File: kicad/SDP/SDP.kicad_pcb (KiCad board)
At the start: 4 copper layers, 164 parts, among them J1 GPIO, J10 Limit, J11 Conn_01x07, J12 Conn_01x07, J13 Conn_01x03, J14 Conn_01x03, J15 Conn_01x02, J16 Conn_01x02, J17 Conn_01x04, J18 Conn_01x04, J19 Conn_01x04, J2 SPI, J20 Conn_01x04, J21 Conn_01x04, J22 Conn_01x04, J23 Conn_01x02, J24 POWER, J25 Conn_01x04, J3 UART, J4 I2C, J5 Conn_01x04, J6 Conn_01x04, J7 RJ25, J8 Conn_01x07, J9 Conn_01x07, Q1 IRLZ44N, Q2 IRLZ44N, Q3 IRLZ44N, SW1 SW_Push_Dual, U1 TPS54233, U2 TPS54233, U3 PIC24FJ128GA010-I/PT, U4 DS3231SN-T&R, Y1 8MHz, Y2 32.768kHz

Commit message: PCB layout and schematic updates
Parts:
- added J26: Conn_01x02, TerminalBlock_Phoenix:TerminalBlock_Phoenix_PT-1,5-2-5.0-H_1x02_P5.00mm_Horizontal, F.Cu at (153.5, 50.2)
- D6, D7, D8: value 1N4007 -> SS1200; footprint Diode_THT:D_DO-41_SOD81_P10.16mm_Horizontal -> Diode_SMD:D_SMA
- J1: footprint Connector_PinSocket_2.54mm:PinSocket_2x12_P2.54mm_Vertical -> Connector_PinSocket_2.54mm:PinSocket_2x09_P2.54mm_Vertical
- Q1, Q2, Q3: footprint Package_TO_SOT_THT:TO-220-3_Vertical -> Package_TO_SOT_SMD:TO-263-2
- moved J11 365.1 mm to (55.3, 135.8)
- moved J12 365.1 mm to (64.5, 135.8)
- moved J8 365.1 mm to (59.9, 135.8)
- moved J9 365.1 mm to (50.7, 135.8)
- moved R18 359.3 mm to (64.9, 99.4), turned to -90 degrees
- moved J6 351.9 mm to (69.0, 160.8)
- moved R22 338.0 mm to (101.6, 90.7), turned to 90 degrees
- moved J13 336.3 mm to (80.5, 162.8)
- moved J14 336.3 mm to (85.1, 162.8)
- moved J10 336.1 mm to (96.5, 85.5), turned to 90 degrees
- moved R23 335.6 mm to (104.1, 90.7), turned to 90 degrees
- moved R24 332.8 mm to (106.7, 90.7), turned to 90 degrees
- moved R21 329.5 mm to (99.1, 90.7), turned to 90 degrees
- moved R20 327.6 mm to (96.5, 90.7), turned to 90 degrees
- moved C22 326.2 mm to (65.4, 162.1), turned to -90 degrees
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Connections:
- J1 pad 1: P21_RB4 -> P19_RE9
- J1 pad 10: P97_RG13 -> P68_RD8
- J1 pad 11: P95_RG14 -> P67_RA15
- J1 pad 12: P1_RG15 -> P69_RD9
- J1 pad 13: P66_RA14 -> P70_RD10
- J1 pad 14: P67_RA15 -> P71_RD11
- J1 pad 15: P93_RE0 -> P89_RG1
- J1 pad 16: P94_RE1 -> P90_RG0
- J1 pad 17: P98_RE2 -> P93_RE0
- J1 pad 18: P99_RE3 -> P94_RE1
- J1 pad 2: P20_RB5 -> P18_RE8
- J1 pad 3: P68_RD8 -> P21_RB4
- J1 pad 4: P69_RD9 -> P20_RB5
- J1 pad 5: P70_RD10 -> P1_RG15
- J1 pad 6: P71_RD11 -> P3_RE5
- J1 pad 7: P90_RG0 -> P4_RE6
- J1 pad 8: P89_RG1 -> P5_RE7
- J1 pad 9: P96_RG12 -> P66_RA14
- J10 pad 1: P93_LIMIT -> P100_LIMIT
- J10 pad 11: P93_LIMIT -> P95_LIMIT
- J10 pad 3: P93_LIMIT -> P99_LIMIT
- J10 pad 5: P93_LIMIT -> P98_LIMIT
- J10 pad 7: P93_LIMIT -> P97_LIMIT
- J10 pad 9: P93_LIMIT -> P96_LIMIT
- J2 pad 2: P53_SDO1 -> P14_SS2
- J2 pad 3: P54_SDI1 -> P53_SDO1
- J2 pad 4: P55_SCK1 -> P12_SDO2
- J2 pad 5: P14_SS2 -> P54_SDI1
- J2 pad 6: P12_SDO2 -> P11_SDI2
- J2 pad 7: P11_SDI2 -> P55_SCK1
- J24 pad 2: +3V3 -> GND
- J24 pad 4: +3V3 -> GND
- J24 pad 5: GND -> +3V3
- J24 pad 7: GND -> +3V3
- J3 pad 2: P49_U2RX -> P51_U1TX
- J3 pad 3: P48_U1RTS -> P49_U2RX
- J3 pad 4: P47_U1CTS -> P52_U1RX
- J3 pad 5: P51_U1TX -> P48_U1RTS
- J3 pad 6: P52_U1RX -> P39_U2RTS
- J3 pad 7: P39_U2RTS -> P47_U1CTS
- J4 pad 2: P57_SCL1 -> P59_SDA2
- J4 pad 3: P59_SDA2 -> P57_SCL1
- R20 pad 2: P93_LIMIT -> P100_LIMIT
- R21 pad 2: P93_LIMIT -> P99_LIMIT
- R22 pad 2: P93_LIMIT -> P98_LIMIT
- R23 pad 2: P93_LIMIT -> P97_LIMIT
- R24 pad 2: P93_LIMIT -> P96_LIMIT
- R25 pad 2: P93_LIMIT -> P95_LIMIT
- U3 pad 100: P100_RE4 -> P100_LIMIT
- U3 pad 95: P95_RG14 -> P95_LIMIT
- U3 pad 96: P96_RG12 -> P96_LIMIT
- U3 pad 97: P97_RG13 -> P97_LIMIT
- U3 pad 98: P98_RE2 -> P98_LIMIT
- U3 pad 99: P99_RE3 -> P99_LIMIT

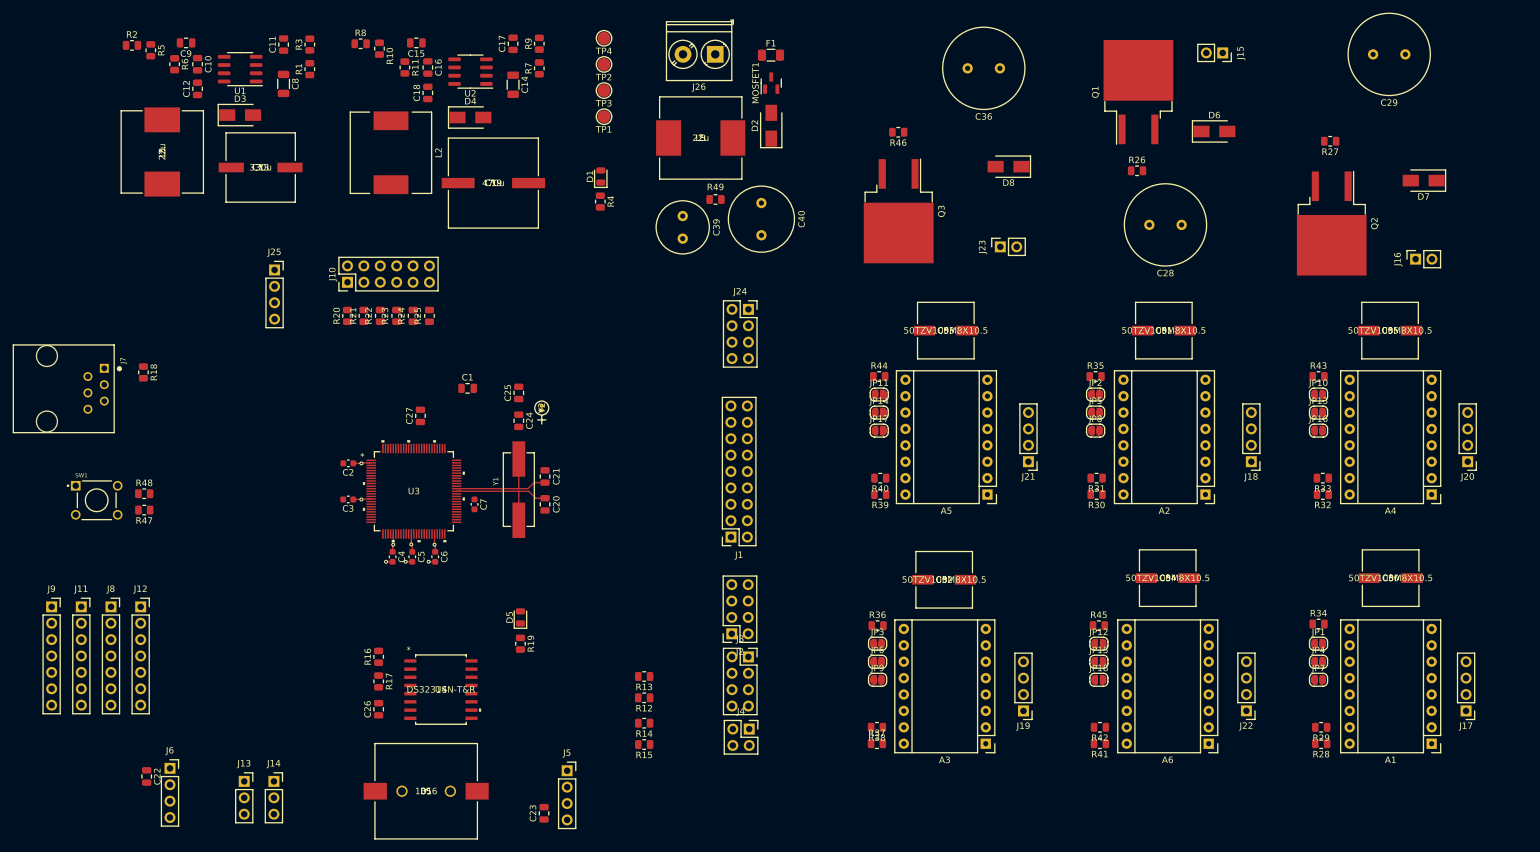
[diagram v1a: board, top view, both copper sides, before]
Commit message: Separated control and motor boards
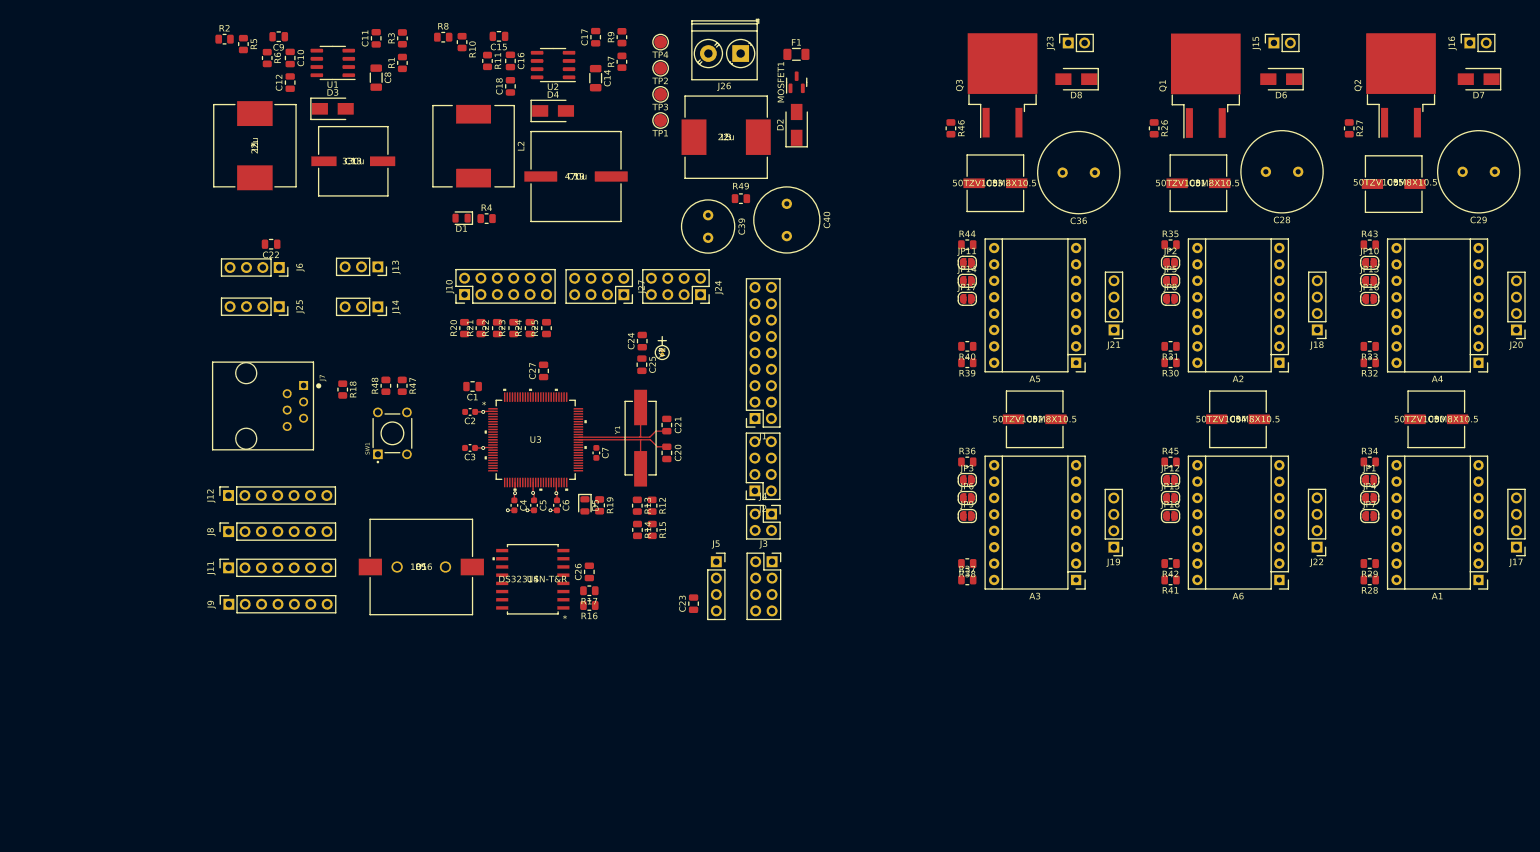
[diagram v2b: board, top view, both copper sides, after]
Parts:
- added J27: MOTOR, Connector_PinSocket_2.54mm:PinSocket_2x04_P2.54mm_Vertical, F.Cu at (139.3, 87.4)
- moved C22 84.7 mm to (84.7, 79.6), turned to 180 degrees
- moved J13 82.4 mm to (101.2, 83.1), turned to -90 degrees
- moved J6 79.4 mm to (85.9, 83.2), turned to -90 degrees
- moved J14 75.3 mm to (101.2, 89.3), turned to -90 degrees
- moved SW1 47.0 mm to (103.5, 108.9), turned to 90 degrees
- moved R47 44.4 mm to (105.0, 101.5), turned to -90 degrees
- moved R48 41.0 mm to (102.5, 101.5), turned to 90 degrees
- moved C23 39.9 mm to (150.1, 135.3)
- moved J5 39.8 mm to (153.7, 128.8)
- moved C26 39.0 mm to (134.0, 130.4)
- moved R17 35.5 mm to (134.0, 133.3), turned to 180 degrees
- moved B1 34.8 mm to (108.0, 129.6)
- moved J16 34.5 mm to (270.4, 48.4)
- moved R16 33.6 mm to (134.0, 135.6), turned to 180 degrees
- moved J4 33.5 mm to (162.2, 121.4)
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
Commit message: PCB layout of main controller board
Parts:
- removed A1, A2, A3, A4, A5, A6: Pololu_Breakout_A4988, Module:Pololu_Breakout-16_15.2x20.3mm
- removed C28, C29, C36: 470u, Capacitor_THT:C_Radial_D12.5mm_H20.0mm_P5.00mm
- removed C30, C31, C32, C33, C34, C35: 50TZV100M8X10.5, 50TZV100M:50TZV100M8X10.5
- removed D6, D7, D8: SS1200, Diode_SMD:D_SMA
- removed J15, J16, J23: Conn_01x02, Connector_PinSocket_2.54mm:PinSocket_1x02_P2.54mm_Vertical
- removed J17, J18, J19, J20, J21, J22: Conn_01x04, Connector_PinHeader_2.54mm:PinHeader_1x04_P2.54mm_Vertical
- removed JP1, JP10, JP11, JP12, JP2, JP3: JP_MS1, Jumper:SolderJumper-2_P1.3mm_Open_RoundedPad1.0x1.5mm
- removed JP13, JP14, JP15, JP4, JP5, JP6: JP_MS2, Jumper:SolderJumper-2_P1.3mm_Open_RoundedPad1.0x1.5mm
- removed JP16, JP17, JP18, JP7, JP8, JP9: JP_MS3, Jumper:SolderJumper-2_P1.3mm_Open_RoundedPad1.0x1.5mm
- removed Q1, Q2, Q3: IRLZ44N, Package_TO_SOT_SMD:TO-263-2
- removed R26, R27, R28, R29, R30, R31, R32, R33, R37, R38, R39, R40, R41, R42, R46: 10k, Resistor_SMD:R_0805_2012Metric
- removed R34, R35, R36, R43, R44, R45: 100k, Resistor_SMD:R_0805_2012Metric
- added H1: MountingHole_Pad, MountingHole:MountingHole_3.2mm_M3_Pad, F.Cu at (77.5, 49.5)
- added H2: MountingHole_Pad, MountingHole:MountingHole_3.2mm_M3_Pad, F.Cu at (166.5, 49.5)
- added H3: MountingHole_Pad, MountingHole:MountingHole_3.2mm_M3_Pad, F.Cu at (166.5, 138.5)
- added H4: MountingHole_Pad, MountingHole:MountingHole_3.2mm_M3_Pad, F.Cu at (77.5, 138.5)
- J27: footprint Connector_PinSocket_2.54mm:PinSocket_2x04_P2.54mm_Vertical -> Connector_PinSocket_2.54mm:PinSocket_2x08_P2.54mm_Vertical
- moved J27 52.8 mm to (133.0, 139.9)
- moved J24 52.7 mm to (145.7, 139.9)
- moved R25 50.2 mm to (97.5, 132.9), turned to -90 degrees
- moved J10 50.1 mm to (110.2, 137.3), turned to -90 degrees
- moved R24 47.3 mm to (100.0, 132.9), turned to -90 degrees
- moved R23 44.9 mm to (102.5, 132.9), turned to -90 degrees
- moved C39 43.7 mm to (108.7, 75.7)
- moved R22 42.9 mm to (105.1, 132.9), turned to -90 degrees
- moved R49 42.4 mm to (115.1, 73.9)
- moved L3 42.1 mm to (113.1, 63.2)
- moved C40 41.7 mm to (122.9, 74.0)
- moved R21 41.4 mm to (107.6, 132.9), turned to -90 degrees
- moved R20 40.6 mm to (110.2, 132.9), turned to -90 degrees
- moved D2 39.9 mm to (126.3, 63.2), turned to 0 degrees
- moved TP4 38.1 mm to (165.0, 80.8), turned to 90 degrees
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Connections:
- J27 pad 1: P72_FAN -> +3V3
- J27 pad 2: P76_EN -> +3V3
- J27 pad 3: P77_STEP -> P72_FAN
- J27 pad 4: P78_DIR -> P76_EN
- J27 pad 5: P79_EN -> P77_STEP
- J27 pad 6: P80_STEP -> P78_DIR
- J27 pad 7: P81_DIR -> P79_EN
- J27 pad 8: P82_EN -> P80_STEP
- J4 pad 1: P56_SDA1 -> P59_SDA2
- J4 pad 2: P59_SDA2 -> P57_SCL1
- J4 pad 3: P57_SCL1 -> P58_SCL2
- J4 pad 4: P58_SCL2 -> P56_SDA1
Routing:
- net P57_SCL1: track 0.00 -> 143.8 mm, vias 0 -> 1
- net P56_SDA1: track 0.00 -> 139.3 mm, vias 0 -> 1
- net P44_TOF4_GPIO1: track 0.00 -> 77.1 mm, vias 0 -> 1
- net P95_LIMIT: track 0.00 -> 72.9 mm, vias 0 -> 2
- net P96_LIMIT: track 0.00 -> 69.7 mm, vias 0 -> 2
- net P35_TOF4_CE: track 0.00 -> 66.6 mm, vias 0 -> 1
- net P97_LIMIT: track 0.00 -> 66.4 mm, vias 0 -> 2
- net P43_TOF3_GPIO1: track 0.00 -> 66.2 mm, vias 0 -> 1
- net P34_TOF3_CE: track 0.00 -> 65.6 mm, vias 0 -> 1
- net P42_TOF2_GPIO1: track 0.00 -> 64.6 mm, vias 0 -> 1
- net P98_LIMIT: track 0.00 -> 62.5 mm, vias 0 -> 2
- net P99_LIMIT: track 0.00 -> 61.0 mm, vias 0 -> 2
- net P41_TOF1_GPIO1: track 0.00 -> 60.4 mm, vias 0 -> 1
- net P100_LIMIT: track 0.00 -> 59.9 mm, vias 0 -> 2
- net P33_TOF2_CE: track 0.00 -> 54.4 mm, vias 0 -> 1
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- added copper zone on In2.Cu, net +3V3
- added copper zone on F.Cu, net GND
- added copper zone on In1.Cu, net GND
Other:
- board outline added: 98 x 98 mm

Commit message: Controller PCB layout
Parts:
- removed J2: SPI, Connector_PinSocket_2.54mm:PinSocket_2x04_P2.54mm_Vertical
- moved R5 120.2 mm to (167.9, 133.0), turned to 180 degrees
- moved R2 117.6 mm to (168.7, 130.0), turned to -90 degrees
- moved C9 117.5 mm to (159.7, 139.3), turned to 0 degrees
- moved R9 115.1 mm to (83.3, 137.7), turned to -90 degrees
- moved R6 114.3 mm to (161.5, 135.5), turned to 90 degrees
- moved C17 112.6 mm to (86.8, 137.7), turned to -90 degrees
- moved R7 109.8 mm to (83.3, 134.0), turned to -90 degrees
- moved C10 109.6 mm to (158.0, 135.5), turned to 90 degrees
- moved C12 103.9 mm to (158.0, 131.7), turned to -90 degrees
- moved C14 103.6 mm to (86.8, 131.7), turned to 90 degrees
- moved U2 101.1 mm to (92.5, 134.9), turned to 0 degrees
- moved U1 100.6 mm to (151.2, 135.2), turned to 0 degrees
- moved C11 100.2 mm to (144.4, 139.0), turned to -90 degrees
- moved C15 99.8 mm to (101.0, 139.1), turned to 0 degrees
- moved L1 98.1 mm to (163.1, 121.0), turned to 90 degrees
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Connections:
- J1 pad 1: P19_RE9 -> P21_RB4
- J1 pad 10: P68_RD8 -> P71_RD11
- J1 pad 11: P67_RA15 -> P5_RE7
- J1 pad 12: P69_RD9 -> P4_RE6
- J1 pad 13: P70_RD10 -> P3_RE5
- J1 pad 14: P71_RD11 -> P1_RG15
- J1 pad 15: P89_RG1 -> P93_RE0
- J1 pad 16: P90_RG0 -> P94_RE1
- J1 pad 17: P93_RE0 -> P89_RG1
- J1 pad 18: P94_RE1 -> P90_RG0
- J1 pad 2: P18_RE8 -> P20_RB5
- J1 pad 3: P21_RB4 -> P19_RE9
- J1 pad 4: P20_RB5 -> P18_RE8
- J1 pad 5: P1_RG15 -> P66_RA14
- J1 pad 6: P3_RE5 -> P67_RA15
- J1 pad 7: P4_RE6 -> P68_RD8
- J1 pad 8: P5_RE7 -> P69_RD9
- J1 pad 9: P66_RA14 -> P70_RD10
- J11 pad 6: P34_TOF3_CE -> P41_TOF3_CE
- J11 pad 7: P43_TOF3_GPIO1 -> P42_TOF3_GPIO1
- J12 pad 6: P35_TOF4_CE -> P43_TOF4_CE
- J3 pad 1: P50_U2TX -> P51_U1TX
- J3 pad 2: P51_U1TX -> P50_U2TX
- J3 pad 3: P49_U2RX -> P52_U1RX
- J3 pad 4: P52_U1RX -> P49_U2RX
- J4 pad 1: P59_SDA2 -> P58_SCL2
- J4 pad 3: P58_SCL2 -> P59_SDA2
- J8 pad 6: P33_TOF2_CE -> P34_TOF2_CE
- J8 pad 7: P42_TOF2_GPIO1 -> P35_TOF2_GPIO1
- J9 pad 7: P41_TOF1_GPIO1 -> P33_TOF1_GPIO1
- U3 pad 33: P33_TOF2_CE -> P33_TOF1_GPIO1
- U3 pad 34: P34_TOF3_CE -> P34_TOF2_CE
- U3 pad 35: P35_TOF4_CE -> P35_TOF2_GPIO1
- U3 pad 41: P41_TOF1_GPIO1 -> P41_TOF3_CE
- U3 pad 42: P42_TOF2_GPIO1 -> P42_TOF3_GPIO1
- U3 pad 43: P43_TOF3_GPIO1 -> P43_TOF4_CE
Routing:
- net +5V: track 0.00 -> 81.3 mm, vias 0 -> 1
- net P35_TOF4_CE: track 66.6 -> 0.00 mm, vias 1 -> 0
- net P43_TOF3_GPIO1: track 66.2 -> 0.00 mm, vias 1 -> 0
- net P34_TOF3_CE: track 65.6 -> 0.00 mm, vias 1 -> 0
- net P42_TOF2_GPIO1: track 64.6 -> 0.00 mm, vias 1 -> 0
- net GND: track 19.2 -> 82.1 mm, vias 17 -> 61
- net P41_TOF1_GPIO1: track 60.4 -> 0.00 mm, vias 1 -> 0
- net P43_TOF4_CE: track 0.00 -> 55.9 mm, vias 0 -> 1
- net P33_TOF2_CE: track 54.4 -> 0.00 mm, vias 1 -> 0
- net P39_U2RTS: track 0.00 -> 53.7 mm, vias 0 -> 1
- net P66_RA14: track 0.00 -> 53.0 mm, vias 0 -> 1
- net P40_U2CTS: track 0.00 -> 52.9 mm, vias 0 -> 1
- net P41_TOF3_CE: track 0.00 -> 52.3 mm, vias 0 -> 1
- net P95_LIMIT: track 72.9 -> 21.4 mm, vias 2 -> 0
- net P34_TOF2_CE: track 0.00 -> 50.1 mm, vias 0 -> 1
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- added copper zone on F.Cu, net +12V
- added copper zone on F.Cu, net Net-(D2-Pad1)
- added copper zone on F.Cu, net Net-(F1-Pad2)

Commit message: Added proximity sensor headers
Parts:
- added J15: Conn_01x03, Connector_PinSocket_2.54mm:PinSocket_1x03_P2.54mm_Vertical, F.Cu at (89.3, 48.4)
- added J16: Conn_01x03, Connector_PinSocket_2.54mm:PinSocket_1x03_P2.54mm_Vertical, F.Cu at (98.7, 48.4)
- added J17: Conn_01x03, Connector_PinSocket_2.54mm:PinSocket_1x03_P2.54mm_Vertical, F.Cu at (94.0, 48.4)
- added J2: Conn_01x03, Connector_PinSocket_2.54mm:PinSocket_1x03_P2.54mm_Vertical, F.Cu at (84.6, 48.4)
- J1: footprint Connector_PinSocket_2.54mm:PinSocket_2x09_P2.54mm_Vertical -> Connector_PinSocket_2.54mm:PinSocket_2x07_P2.54mm_Vertical
- moved J24 9.41 mm to (152.0, 50.9)
- moved J4 9.41 mm to (159.6, 50.9)
- moved R21 9.41 mm to (106.3, 55.3)
- moved R23 9.41 mm to (111.4, 55.3)
- moved J10 9.41 mm to (103.8, 50.9)
- moved R20 9.41 mm to (103.8, 55.3)
- moved R22 9.41 mm to (108.8, 55.3)
- moved R24 9.41 mm to (113.9, 55.3)
- moved R25 9.41 mm to (116.5, 55.3)
- moved J27 9.41 mm to (139.3, 50.9)
- moved C24 1.40 mm to (130.3, 61.0)
- moved C25 1.40 mm to (134.0, 61.0)
- moved Y2 1.40 mm to (131.9, 58.3)
- moved C23 1.40 mm to (89.0, 88.0)
- moved J5 1.37 mm to (85.6, 81.7)
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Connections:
- U3 pad 89: P89_RG1 -> P89_PROX4
- U3 pad 90: P90_RG0 -> P90_PROX3
- U3 pad 93: P93_RE0 -> P93_PROX2
- U3 pad 94: P94_RE1 -> P94_PROX1
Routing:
- net +12V: track 11.4 -> 63.2 mm, vias 2 -> 5
- net P89_RG1: track 51.4 -> 0.00 mm, vias 1 -> 0
- net P91_TEMP1: track 10.4 -> 58.3 mm, vias 0 -> 1
- net P90_RG0: track 47.9 -> 0.00 mm, vias 1 -> 0
- net P93_RE0: track 46.6 -> 0.00 mm, vias 1 -> 0
- net P94_RE1: track 43.6 -> 0.00 mm, vias 1 -> 0
- net P92_TEMP2: track 10.4 -> 53.2 mm, vias 0 -> 1
- net P94_PROX1: track 0.00 -> 41.2 mm, vias 0 -> 1
- net P93_PROX2: track 0.00 -> 37.1 mm, vias 0 -> 1
- net GND: track 82.1 -> 118.9 mm, vias 61 -> 83
- net P90_PROX3: track 0.00 -> 35.0 mm, vias 0 -> 1
- net P89_PROX4: track 0.00 -> 30.8 mm, vias 0 -> 1
- net P72_FAN: track 0.00 -> 24.0 mm
- net +3V3: track 85.1 -> 97.9 mm, vias 27 -> 34
- net P99_LIMIT: track 29.9 -> 20.3 mm
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
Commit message: Motor PCB layout
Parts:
- removed the TP1 at (158.1, 109.9)
- removed the TP2 at (150.0, 109.9)
- added J18: 12V, Connector_PinSocket_2.54mm:PinSocket_2x02_P2.54mm_Vertical, F.Cu at (150.7, 107.5)
- TP1: renamed from TP3; footprint TestPoint:TestPoint_Pad_D2.0mm -> TestPoint:TestPoint_Keystone_5005-5009_Compact
- TP2: renamed from TP4; footprint TestPoint:TestPoint_Pad_D2.0mm -> TestPoint:TestPoint_Keystone_5005-5009_Compact
- moved TP2 84.1 mm to (81.9, 55.5)
- moved C13 4.40 mm to (152.3, 119.1)
- moved D2 4.40 mm to (121.1, 124.3)
- moved J12 4.40 mm to (171.4, 101.5)
- moved L1 4.40 mm to (167.4, 120.1)
- moved R13 4.40 mm to (149.9, 76.8)
- moved R14 4.40 mm to (149.8, 90.8)
- moved C24 4.40 mm to (134.7, 60.1)
- moved C25 4.40 mm to (138.3, 60.1)
- moved H2 4.40 mm to (170.8, 48.7)
- moved J13 4.40 mm to (165.8, 63.4)
- moved J2 4.40 mm to (88.9, 47.5)
- moved J4 4.40 mm to (163.9, 50.1)
- moved Y2 4.40 mm to (136.2, 57.4)
- moved C10 4.40 mm to (162.3, 134.7)
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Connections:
- J27 pad 15: +12V -> GND
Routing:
- net GND: track 118.9 -> 128.4 mm, vias 83 -> 90
- net +3V3: track 97.9 -> 94.0 mm, vias 34 -> 46
- net +12V: track 63.2 -> 59.5 mm, vias 5 -> 3
- net Net-(D5-Pad1): track 0.00 -> 2.30 mm
- added copper zone on B.Cu, net +12V
- added copper zone on F.Cu, net +3V3
